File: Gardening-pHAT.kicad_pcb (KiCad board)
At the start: 2 copper layers, 65 x 30 mm, 26 parts, among them P1 CONN_01X03, P2 CONN_01X03, P3 CONN_01X03, P4 CONN_02X05, U1 CAT24C32WI-GT3, U2 MCP3002

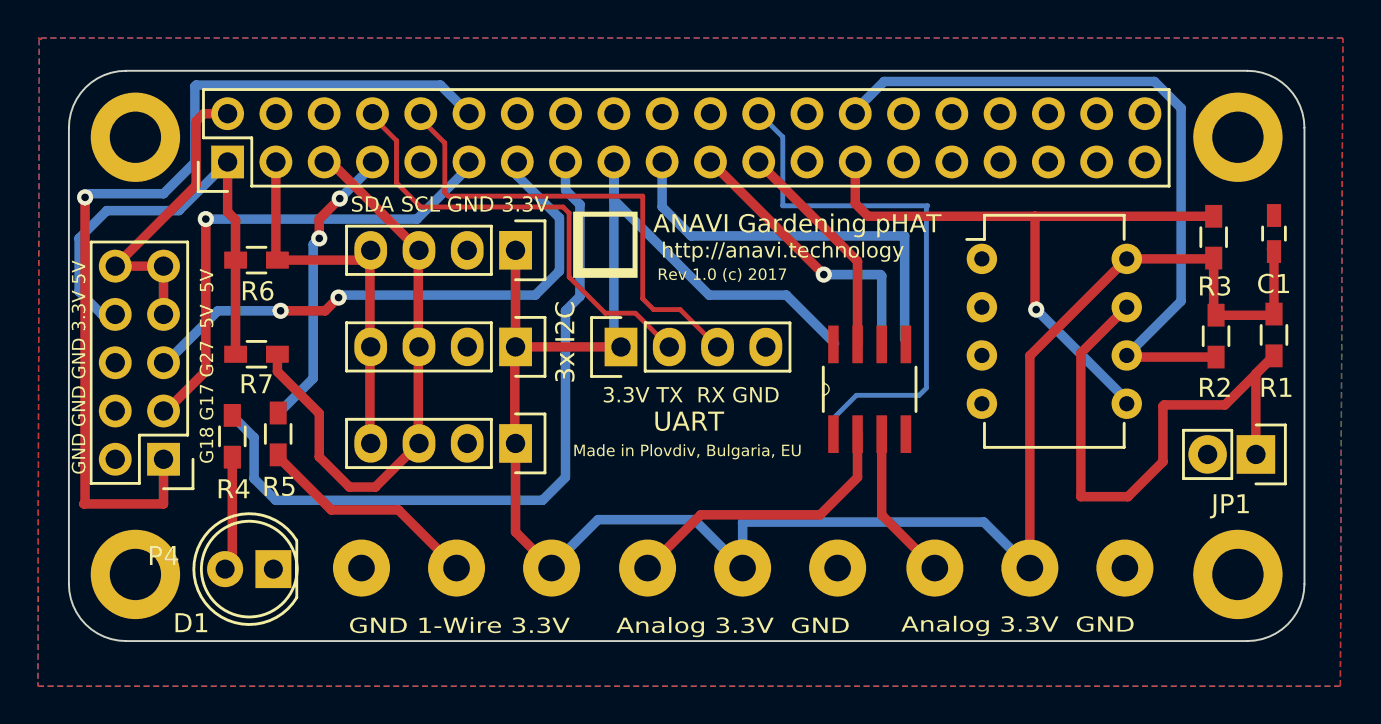
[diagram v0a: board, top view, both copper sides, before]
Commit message: Remove one I2C slot and change labels
Leave only two I2C slots to ensure that there is
enough space for the labels. Fix wiring issues.

Signed-off-by: Leon Anavi <leon@anavi.org>
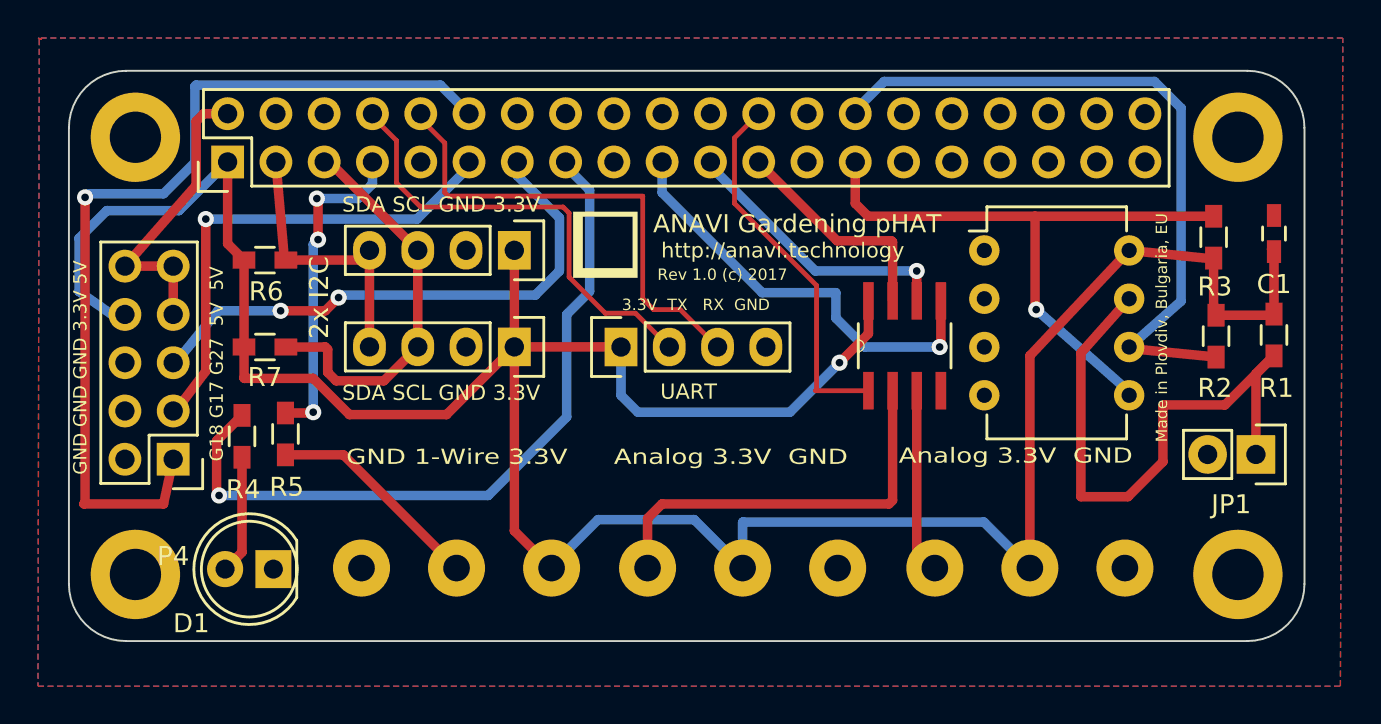
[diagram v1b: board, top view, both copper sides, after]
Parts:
- removed SENS3: I2C_SENS_1, Pin_Headers:Pin_Header_Straight_1x04
- moved SENS2 5.08 mm to (171.9, 84.4)
- moved SENS1 5.08 mm to (171.9, 89.5)
- moved U2 2.94 mm to (192.5, 89.5)
- moved R7 0.59 mm to (158.8, 89.5)
- moved P4 0.51 mm to (154.0, 95.4)
- moved R4 0.51 mm to (157.6, 94.2)
- moved U1 0.46 mm to (196.7, 84.5)
- moved R6 0.44 mm to (158.8, 85.0)
- moved R5 0.38 mm to (159.9, 94.1)
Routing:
- net +3V3: track 140.0 -> 152.5 mm, vias 0 -> 1
- net Net-(R7-Pad2): track 31.8 -> 22.5 mm
- net Net-(RASP_CONN1-Pad24): track 28.3 -> 19.7 mm
- net Net-(P3-Pad1): track 15.3 -> 21.7 mm
- net Net-(R6-Pad2): track 20.7 -> 15.1 mm
- net Net-(R5-Pad2): track 15.8 -> 17.9 mm, vias 2 -> 3
- net Net-(RASP_CONN1-Pad19): track 21.2 -> 22.8 mm, vias 0 -> 1
- net Net-(P2-Pad1): track 8.20 -> 9.72 mm
- net Net-(R4-Pad2): track 38.4 -> 39.3 mm, vias 0 -> 1
- net Net-(D1-Pad2): track 6.04 -> 6.79 mm
- net Net-(R2-Pad2): track 38.1 -> 37.6 mm
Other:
- board text added: "2x I2C"
- board text removed: "3x I2C"
- board text removed: "470"

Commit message: Gardening-pHAT.kicad_pcb: Move labels
Signed-off-by: Leon Anavi <leon@anavi.org>
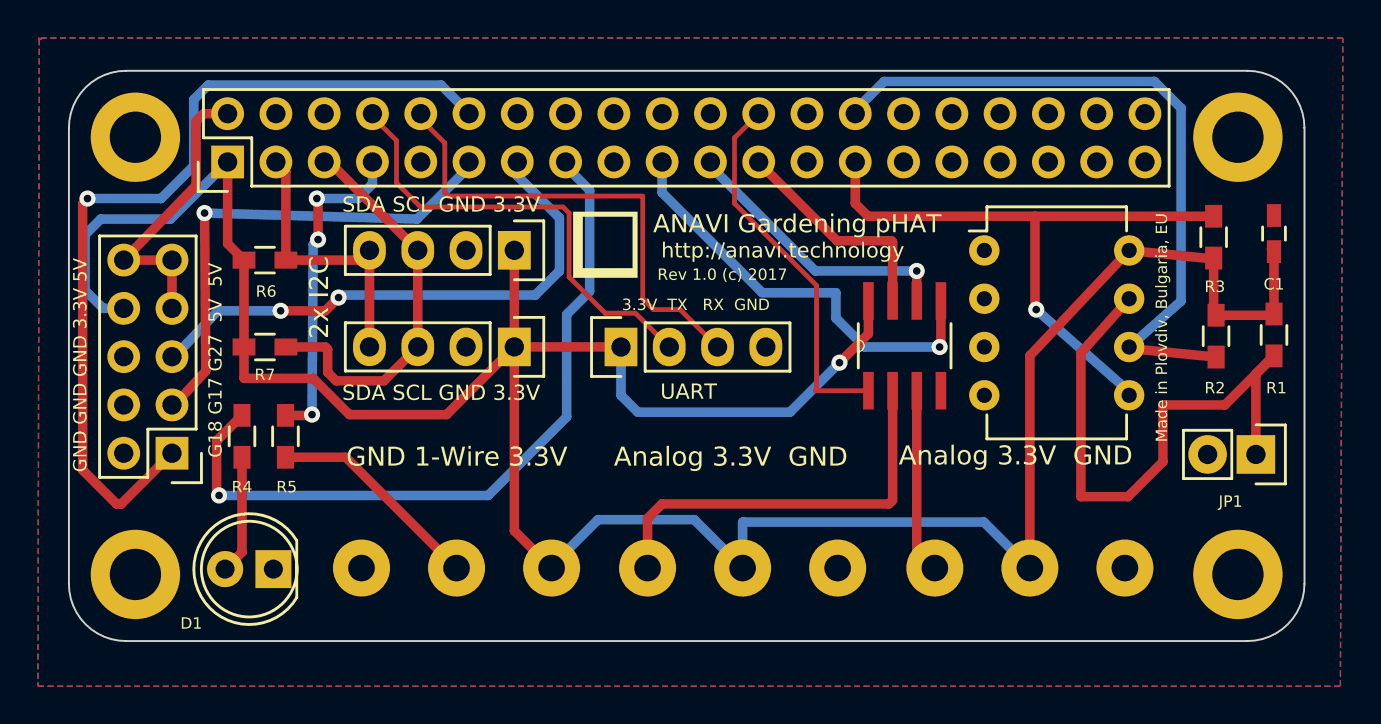
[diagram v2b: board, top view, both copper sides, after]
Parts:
- moved P4 0.32 mm to (153.9, 95.1)
- moved R5 0.13 mm to (159.9, 94.2)
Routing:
- net Net-(P4-Pad1): track 48.4 -> 46.2 mm
- net +3V3: track 152.5 -> 151.8 mm

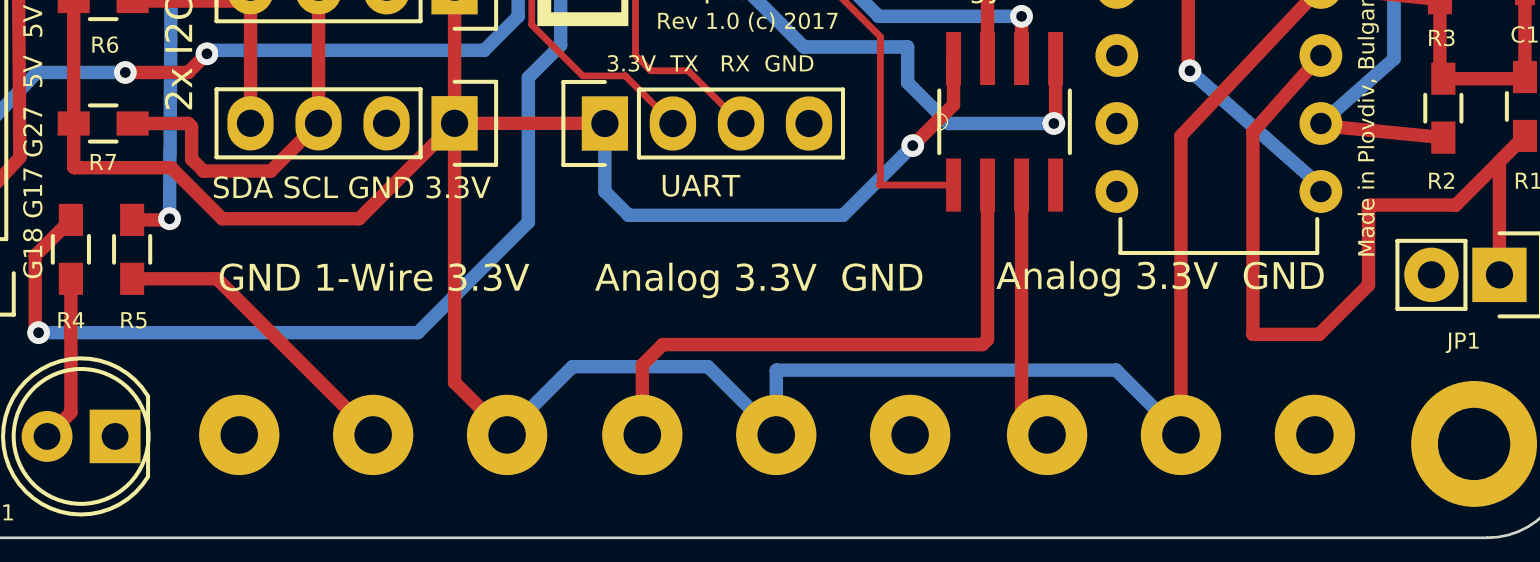
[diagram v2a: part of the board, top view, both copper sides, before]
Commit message: Gardening-pHAT.kicad_pcb: Replace labels
Replace "Analog" with "Signal" and adjust the
position of the labels.

Signed-off-by: Leon Anavi <leon@anavi.org>
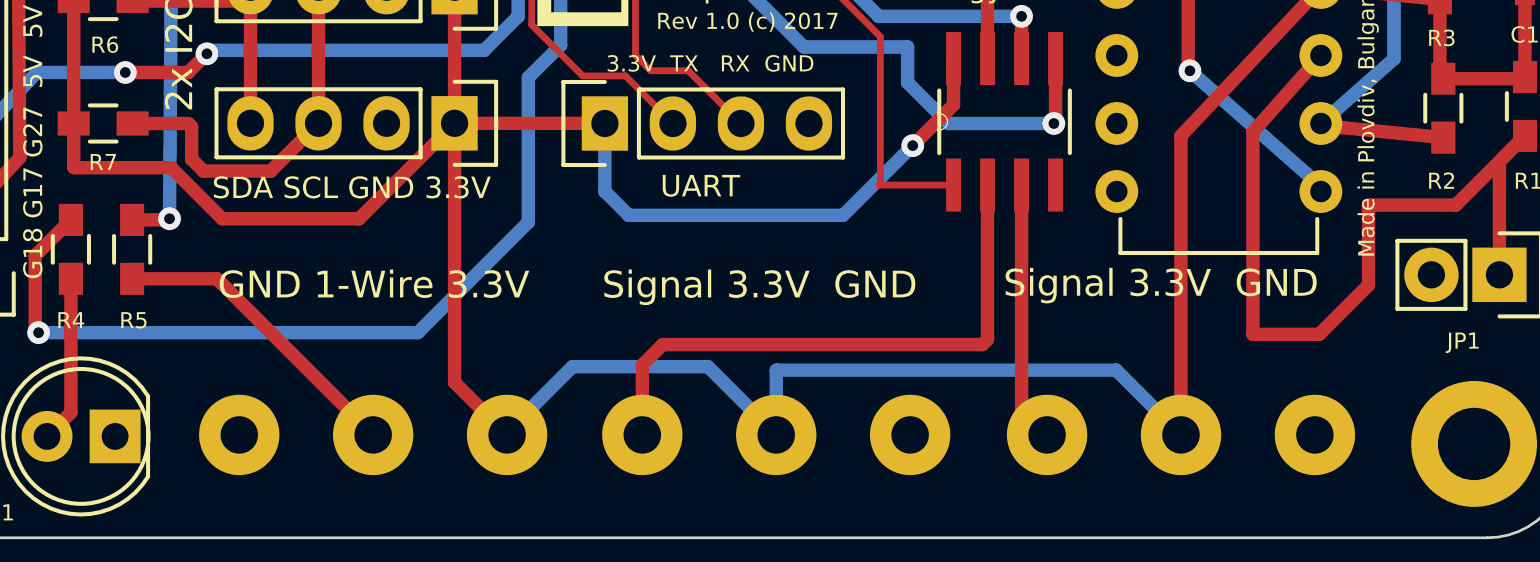
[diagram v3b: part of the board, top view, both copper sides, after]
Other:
- board text added: "Signal 3.3V GND"
- board text removed: "Analog 3.3V GND"
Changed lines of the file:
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@@
     (effects (font (size 0.7 0.7) (thickness 0.175)))
   )
-  (gr_text "Analog 3.3V  GND" (at 198.3105 95.25) (layer F.SilkS)
+  (gr_text "Signal 3.3V  GND" (at 198.3105 95.504) (layer F.SilkS)
     (effects (font (size 1 1) (thickness 0.2)))
   )
-  (gr_text "Analog 3.3V  GND" (at 183.3245 95.3135) (layer F.SilkS)
+  (gr_text "Signal 3.3V  GND" (at 183.3245 95.5675) (layer F.SilkS)
     (effects (font (size 1 1) (thickness 0.2)))
   )
-  (gr_text "GND 1-Wire 3.3V" (at 168.91 95.3135) (layer F.SilkS)
+  (gr_text "GND 1-Wire 3.3V" (at 168.91 95.5675) (layer F.SilkS)
     (effects (font (size 1 1) (thickness 0.2)))
   )
